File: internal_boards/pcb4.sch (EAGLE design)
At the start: 9 parts, among them J1 22-27-2021-02, J2 22-27-2021-02

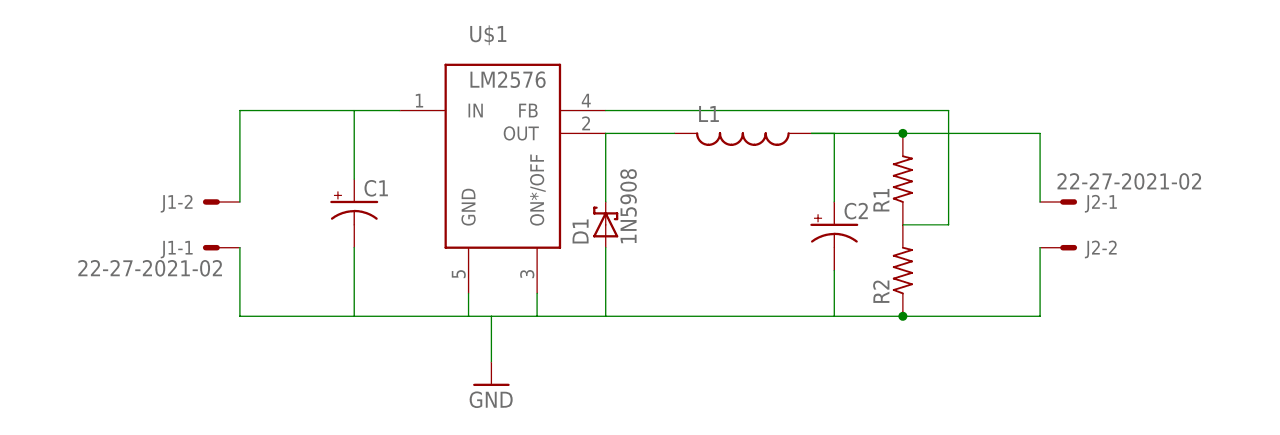
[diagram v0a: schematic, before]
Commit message: * Enhancement to board to use regulator with pins slightly spaced out
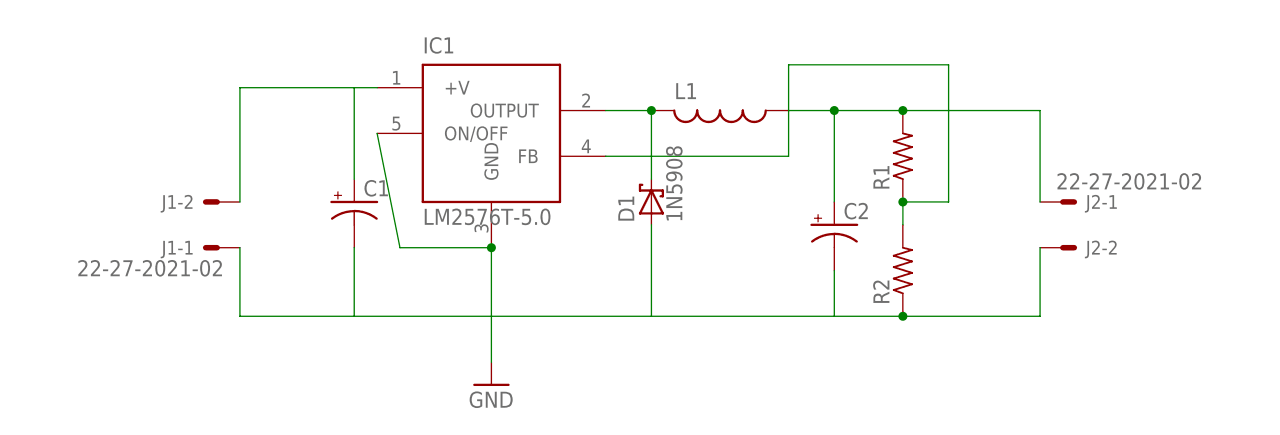
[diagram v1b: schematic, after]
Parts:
- removed U$1: LM2576, LM2576:LM2576
- added IC1: LM2576T-5.0, LM2576:LM2576T-5.0
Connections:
- net GND: now also IC1.GND, IC1.ON/OFF; no longer U$1.GND, U$1.ON*/OFF
- net N$1: now also IC1.FB; no longer U$1.FB
- net N$2: now also IC1.+V; no longer U$1.IN
- net N$3: now also IC1.OUTPUT; no longer U$1.OUT
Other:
- moved on the sheet: D1, L1, R1
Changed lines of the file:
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@@
 <?xml version="1.0" encoding="utf-8"?>
 <!DOCTYPE eagle SYSTEM "eagle.dtd">
-<eagle version="6.5.0">
+<eagle version="7.1.0">
 <drawing>
 <settings>
@@
 </classes>
 <parts>
-<part name="U$1" library="LM2576" deviceset="LM2576" device=""/>
 <part name="GND1" library="supply1" deviceset="GND" device=""/>
 <part name="C1" library="adafruit" deviceset="CPOL-US" device="TT2D6"/>
@@
 <part name="J1" library="con-molex" deviceset="22-?-02" device="27-2021"/>
 <part name="J2" library="con-molex" deviceset="22-?-02" device="27-2021"/>
+<part name="IC1" library="LM2576" deviceset="LM2576*" device="T-5.0"/>
 </parts>
 <sheets>
@@
 </plain>
 <instances>
-<instance part="U$1" gate="G$1" x="38.1" y="55.88"/>
 <instance part="GND1" gate="1" x="35.56" y="27.94"/>
 <instance part="C1" gate="G$1" x="20.32" y="48.26"/>
-<instance part="D1" gate="1" x="48.26" y="45.72" rot="R90"/>
-<instance part="L1" gate="G$1" x="63.5" y="55.88" rot="R270"/>
-<instance part="R1" gate="G$1" x="81.28" y="50.8" rot="R90"/>
+<instance part="D1" gate="1" x="53.34" y="48.26" rot="R90"/>
+<instance part="L1" gate="G$1" x="60.96" y="58.42" rot="R270"/>
+<instance part="R1" gate="G$1" x="81.28" y="53.34" rot="R90"/>
 <instance part="R2" gate="G$1" x="81.28" y="40.64" rot="R90"/>
 <instance part="C2" gate="G$1" x="73.66" y="45.72"/>
@@
 <instance part="J2" gate="-1" x="99.06" y="48.26"/>
 <instance part="J2" gate="-2" x="99.06" y="43.18"/>
+<instance part="IC1" gate="G$1" x="27.94" y="48.26"/>
 </instances>
 <busses>
@@
 <net name="GND" class="0">
 <segment>
-<pinref part="U$1" gate="G$1" pin="GND"/>
-<wire x1="33.02" y1="38.1" x2="33.02" y2="35.56" width="0.1524" layer="91"/>
-<pinref part="U$1" gate="G$1" pin="ON*/OFF"/>
-<wire x1="33.02" y1="35.56" x2="35.56" y2="35.56" width="0.1524" layer="91"/>
-<wire x1="35.56" y1="35.56" x2="40.64" y2="35.56" width="0.1524" layer="91"/>
-<wire x1="40.64" y1="35.56" x2="40.64" y2="38.1" width="0.1524" layer="91"/>
 <wire x1="35.56" y1="35.56" x2="35.56" y2="30.48" width="0.1524" layer="91"/>
 <pinref part="GND1" gate="1" pin="GND"/>
-<wire x1="33.02" y1="35.56" x2="20.32" y2="35.56" width="0.1524" layer="91"/>
+<wire x1="35.56" y1="35.56" x2="20.32" y2="35.56" width="0.1524" layer="91"/>
 <wire x1="20.32" y1="35.56" x2="7.62" y2="35.56" width="0.1524" layer="91"/>
-<wire x1="48.26" y1="35.56" x2="73.66" y2="35.56" width="0.1524" layer="91"/>
+<wire x1="53.34" y1="35.56" x2="73.66" y2="35.56" width="0.1524" layer="91"/>
 <pinref part="D1" gate="1" pin="A"/>
 <wire x1="73.66" y1="35.56" x2="81.28" y2="35.56" width="0.1524" layer="91"/>
 <wire x1="81.28" y1="35.56" x2="96.52" y2="35.56" width="0.1524" layer="91"/>
-<wire x1="48.26" y1="43.18" x2="48.26" y2="35.56" width="0.1524" layer="91"/>
-<wire x1="40.64" y1="35.56" x2="48.26" y2="35.56" width="0.1524" layer="91"/>
+<wire x1="53.34" y1="45.72" x2="53.34" y2="35.56" width="0.1524" layer="91"/>
+<wire x1="35.56" y1="35.56" x2="53.34" y2="35.56" width="0.1524" layer="91"/>
 <pinref part="R2" gate="G$1" pin="1"/>
 <junction x="81.28" y="35.56"/>
@@
 <pinref part="C1" gate="G$1" pin="-"/>
 <wire x1="20.32" y1="43.18" x2="20.32" y2="35.56" width="0.1524" layer="91"/>
+<pinref part="IC1" gate="G$1" pin="ON/OFF"/>
+<wire x1="25.4" y1="43.18" x2="22.86" y2="55.88" width="0.1524" layer="91"/>
+<pinref part="IC1" gate="G$1" pin="GND"/>
+<wire x1="25.4" y1="43.18" x2="35.56" y2="43.18" width="0.1524" layer="91"/>
+<wire x1="35.56" y1="43.18" x2="35.56" y2="35.56" width="0.1524" layer="91"/>
+<junction x="35.56" y="43.18"/>
 </segment>
 </net>
 <net name="N$2" class="0">
 <segment>
-<pinref part="U$1" gate="G$1" pin="IN"/>
-<wire x1="25.4" y1="58.42" x2="20.32" y2="58.42" width="0.1524" layer="91"/>
 <pinref part="J1" gate="-2" pin="S"/>
-<wire x1="20.32" y1="58.42" x2="7.62" y2="58.42" width="0.1524" layer="91"/>
-<wire x1="7.62" y1="58.42" x2="7.62" y2="48.26" width="0.1524" layer="91"/>
+<wire x1="20.32" y1="60.96" x2="7.62" y2="60.96" width="0.1524" layer="91"/>
+<wire x1="7.62" y1="60.96" x2="7.62" y2="48.26" width="0.1524" layer="91"/>
 <pinref part="C1" gate="G$1" pin="+"/>
-<wire x1="20.32" y1="50.8" x2="20.32" y2="58.42" width="0.1524" layer="91"/>
-</segment>
-</net>
-<net name="N$3" class="0">
-<segment>
-<pinref part="U$1" gate="G$1" pin="OUT"/>
-<wire x1="48.26" y1="55.88" x2="55.88" y2="55.88" width="0.1524" layer="91"/>
-<pinref part="D1" gate="1" pin="C"/>
-<wire x1="48.26" y1="48.26" x2="48.26" y2="55.88" width="0.1524" layer="91"/>
-<pinref part="L1" gate="G$1" pin="2"/>
+<wire x1="20.32" y1="50.8" x2="20.32" y2="60.96" width="0.1524" layer="91"/>
+<pinref part="IC1" gate="G$1" pin="+V"/>
+<wire x1="22.86" y1="60.96" x2="20.32" y2="60.96" width="0.1524" layer="91"/>
 </segment>
 </net>
@@
 <pinref part="L1" gate="G$1" pin="1"/>
 <pinref part="R1" gate="G$1" pin="2"/>
-<wire x1="71.12" y1="55.88" x2="81.28" y2="55.88" width="0.1524" layer="91"/>
-<wire x1="81.28" y1="55.88" x2="96.52" y2="55.88" width="0.1524" layer="91"/>
-<junction x="81.28" y="55.88"/>
+<wire x1="73.66" y1="58.42" x2="81.28" y2="58.42" width="0.1524" layer="91"/>
+<wire x1="81.28" y1="58.42" x2="96.52" y2="58.42" width="0.1524" layer="91"/>
+<junction x="81.28" y="58.42"/>
 <pinref part="J2" gate="-1" pin="S"/>
-<wire x1="96.52" y1="55.88" x2="96.52" y2="48.26" width="0.1524" layer="91"/>
+<wire x1="96.52" y1="58.42" x2="96.52" y2="48.26" width="0.1524" layer="91"/>
 <pinref part="C2" gate="G$1" pin="+"/>
-<wire x1="71.12" y1="55.88" x2="73.66" y2="55.88" width="0.1524" layer="91"/>
-<wire x1="73.66" y1="55.88" x2="73.66" y2="48.26" width="0.1524" layer="91"/>
+<wire x1="68.58" y1="58.42" x2="73.66" y2="58.42" width="0.1524" layer="91"/>
+<wire x1="73.66" y1="58.42" x2="73.66" y2="48.26" width="0.1524" layer="91"/>
+<junction x="73.66" y="58.42"/>
 </segment>
 </net>
@@
 <pinref part="R1" gate="G$1" pin="1"/>
 <pinref part="R2" gate="G$1" pin="2"/>
-<wire x1="81.28" y1="45.72" x2="86.36" y2="45.72" width="0.1524" layer="91"/>
-<wire x1="86.36" y1="45.72" x2="86.36" y2="58.42" width="0.1524" layer="91"/>
-<pinref part="U$1" gate="G$1" pin="FB"/>
-<wire x1="86.36" y1="58.42" x2="48.26" y2="58.42" width="0.1524" layer="91"/>
-</segment>
-</net>
+<wire x1="81.28" y1="48.26" x2="86.36" y2="48.26" width="0.1524" layer="91"/>
+<wire x1="86.36" y1="48.26" x2="86.36" y2="63.5" width="0.1524" layer="91"/>
+<junction x="81.28" y="48.26"/>
+<wire x1="81.28" y1="48.26" x2="81.28" y2="45.72" width="0.1524" layer="91"/>
+<wire x1="86.36" y1="63.5" x2="68.58" y2="63.5" width="0.1524" layer="91"/>
+<wire x1="68.58" y1="63.5" x2="68.58" y2="53.34" width="0.1524" layer="91"/>
+<pinref part="IC1" gate="G$1" pin="FB"/>
+<wire x1="68.58" y1="53.34" x2="48.26" y2="53.34" width="0.1524" layer="91"/>
+</segment>
+</net>
+<net name="N$3" class="0">
+<segment>
+<pinref part="IC1" gate="G$1" pin="OUTPUT"/>
+<wire x1="53.34" y1="58.42" x2="48.26" y2="58.42" width="0.1524" layer="91"/>
+<pinref part="D1" gate="1" pin="C"/>
+<wire x1="53.34" y1="50.8" x2="53.34" y2="58.42" width="0.1524" layer="91"/>
+<pinref part="L1" gate="G$1" pin="2"/>
+<junction x="53.34" y="58.42"/>
+</segment>
+</net>

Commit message: * Setting values of components in Schematic.
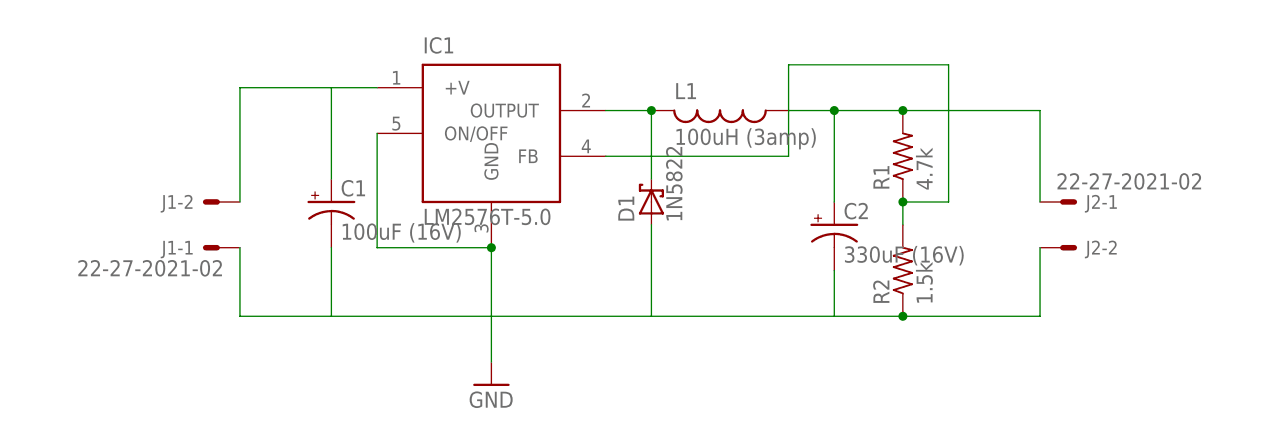
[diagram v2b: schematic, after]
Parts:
- C1: value (none) -> 100uF (16V)
- C2: value (none) -> 330uF (16V)
- D1: value 1N5908 -> 1N5822
- L1: value (none) -> 100uH (3amp)
- R1: value (none) -> 4.7k
- R2: value (none) -> 1.5k
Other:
- moved on the sheet: C1
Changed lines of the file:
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@@
 <parts>
 <part name="GND1" library="supply1" deviceset="GND" device=""/>
-<part name="C1" library="adafruit" deviceset="CPOL-US" device="TT2D6"/>
-<part name="D1" library="diode" deviceset="1N5908" device=""/>
-<part name="L1" library="resistor" deviceset="L-US" device="TJ3-U1"/>
-<part name="R1" library="adafruit" deviceset="R-US_" device="0204/7"/>
-<part name="R2" library="adafruit" deviceset="R-US_" device="0204/7"/>
-<part name="C2" library="adafruit" deviceset="CPOL-US" device="TT5D10"/>
+<part name="C1" library="adafruit" deviceset="CPOL-US" device="TT2D6" value="100uF (16V)"/>
+<part name="D1" library="diode" deviceset="1N5908" device="" value="1N5822"/>
+<part name="L1" library="resistor" deviceset="L-US" device="TJ3-U1" value="100uH (3amp)"/>
+<part name="R1" library="adafruit" deviceset="R-US_" device="0204/7" value="4.7k"/>
+<part name="R2" library="adafruit" deviceset="R-US_" device="0204/7" value="1.5k"/>
+<part name="C2" library="adafruit" deviceset="CPOL-US" device="TT5D10" value="330uF (16V)"/>
 <part name="J1" library="con-molex" deviceset="22-?-02" device="27-2021"/>
 <part name="J2" library="con-molex" deviceset="22-?-02" device="27-2021"/>
@@
 <instances>
 <instance part="GND1" gate="1" x="35.56" y="27.94"/>
-<instance part="C1" gate="G$1" x="20.32" y="48.26"/>
+<instance part="C1" gate="G$1" x="17.78" y="48.26"/>
 <instance part="D1" gate="1" x="53.34" y="48.26" rot="R90"/>
 <instance part="L1" gate="G$1" x="60.96" y="58.42" rot="R270"/>
@@
 <wire x1="35.56" y1="35.56" x2="35.56" y2="30.48" width="0.1524" layer="91"/>
 <pinref part="GND1" gate="1" pin="GND"/>
-<wire x1="35.56" y1="35.56" x2="20.32" y2="35.56" width="0.1524" layer="91"/>
-<wire x1="20.32" y1="35.56" x2="7.62" y2="35.56" width="0.1524" layer="91"/>
+<wire x1="35.56" y1="35.56" x2="17.78" y2="35.56" width="0.1524" layer="91"/>
+<wire x1="17.78" y1="35.56" x2="7.62" y2="35.56" width="0.1524" layer="91"/>
 <wire x1="53.34" y1="35.56" x2="73.66" y2="35.56" width="0.1524" layer="91"/>
 <pinref part="D1" gate="1" pin="A"/>
@@
 <wire x1="73.66" y1="40.64" x2="73.66" y2="35.56" width="0.1524" layer="91"/>
 <pinref part="C1" gate="G$1" pin="-"/>
-<wire x1="20.32" y1="43.18" x2="20.32" y2="35.56" width="0.1524" layer="91"/>
+<wire x1="17.78" y1="43.18" x2="17.78" y2="35.56" width="0.1524" layer="91"/>
 <pinref part="IC1" gate="G$1" pin="ON/OFF"/>
-<wire x1="25.4" y1="43.18" x2="22.86" y2="55.88" width="0.1524" layer="91"/>
+<wire x1="22.86" y1="43.18" x2="22.86" y2="55.88" width="0.1524" layer="91"/>
 <pinref part="IC1" gate="G$1" pin="GND"/>
-<wire x1="25.4" y1="43.18" x2="35.56" y2="43.18" width="0.1524" layer="91"/>
+<wire x1="22.86" y1="43.18" x2="35.56" y2="43.18" width="0.1524" layer="91"/>
 <wire x1="35.56" y1="43.18" x2="35.56" y2="35.56" width="0.1524" layer="91"/>
 <junction x="35.56" y="43.18"/>
@@
 <segment>
 <pinref part="J1" gate="-2" pin="S"/>
-<wire x1="20.32" y1="60.96" x2="7.62" y2="60.96" width="0.1524" layer="91"/>
+<wire x1="17.78" y1="60.96" x2="7.62" y2="60.96" width="0.1524" layer="91"/>
 <wire x1="7.62" y1="60.96" x2="7.62" y2="48.26" width="0.1524" layer="91"/>
 <pinref part="C1" gate="G$1" pin="+"/>
-<wire x1="20.32" y1="50.8" x2="20.32" y2="60.96" width="0.1524" layer="91"/>
+<wire x1="17.78" y1="50.8" x2="17.78" y2="60.96" width="0.1524" layer="91"/>
 <pinref part="IC1" gate="G$1" pin="+V"/>
-<wire x1="22.86" y1="60.96" x2="20.32" y2="60.96" width="0.1524" layer="91"/>
+<wire x1="22.86" y1="60.96" x2="17.78" y2="60.96" width="0.1524" layer="91"/>
 </segment>
 </net>
